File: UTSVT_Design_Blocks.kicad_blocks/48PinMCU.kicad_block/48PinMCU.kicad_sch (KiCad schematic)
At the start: 29 parts, among them J1 SWD_Header_02x02, SW1 SW_SPDT, SW2 Reset, U1 STM32G431CBT6, Y1 Crystal

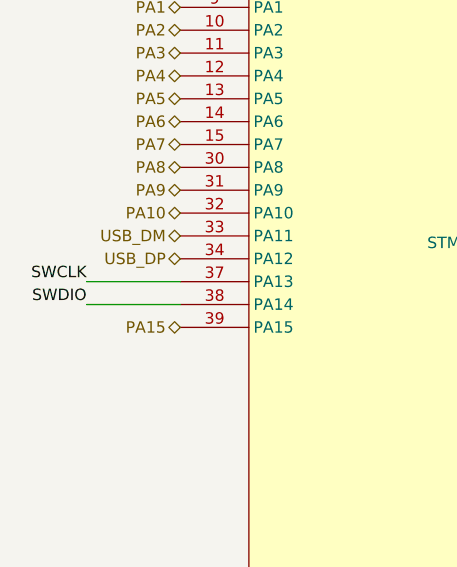
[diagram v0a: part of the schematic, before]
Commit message: 48 pin MCU swd swapped, fixed now
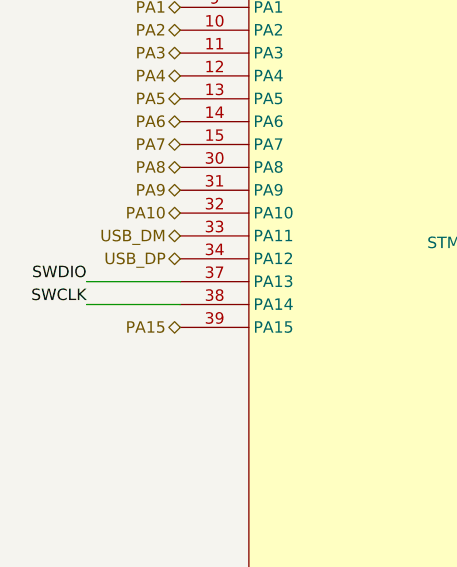
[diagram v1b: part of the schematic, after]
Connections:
- net SWCLK: now also U1.38 (PA14); no longer U1.37 (PA13)
- net SWDIO: now also U1.37 (PA13); no longer U1.38 (PA14)
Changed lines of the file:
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@@
 	)
 	(label "SWCLK"
-		(at 29.972 70.358 180)
+		(at 29.972 72.898 180)
 		(effects
 			(font
@@
 		)
 		(property "Netclass" "Default"
-			(at 29.718 70.358 0)
+			(at 29.718 72.898 0)
 			(effects
 				(font
@@
 	)
 	(label "SWDIO"
-		(at 29.972 72.898 180)
+		(at 29.972 70.358 180)
 		(effects
 			(font
@@
 		)
 		(property "Netclass" "Default"
-			(at 29.718 72.898 0)
+			(at 29.718 70.358 0)
 			(effects
 				(font
